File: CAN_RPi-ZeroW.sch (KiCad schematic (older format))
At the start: 32 parts, among them J1 RJ45, J2 RJ45, J3 Raspberry_Pi_2_3, SW1 SW_SPST, U1 TJA1042T/3, U2 MCP2515-I/ST, U3 MCP16301, Y1 8MHz

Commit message: PCB errors corrected and short installation guide added to README.md
Corrected errors:
- Pin header instead of socket strip used --> wrong pin layout of Raspi connector
- STB pin of transceiver not connected --> sending of messages was not possible

Now, small 26 pin connector is used instead of full 40 pin RPi HAT connector.
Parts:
- removed J3: Raspberry_Pi_2_3, Pin_Headers:Pin_Header_Straight_2x20_Pitch2.54mm, symbol Connector:Raspberry_Pi_2_3
- added J3: Raspberry_Pi_HAT_26p, Socket_Strips:Socket_Strip_Straight_2x13_Pitch2.54mm, symbol LibreSolar:Raspberry_Pi_HAT_26p
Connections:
- net +3V3: now also J3.1 (3V3), J3.17 (3V3)
- net +5V: now also J3.2 (5V), J3.4 (5V)
- net CAN_INT: now also J3.22 (GPIO25_(GEN6))
- net GND: now also J3.14 (GND), J3.20 (GND), J3.25 (GND), J3.6 (GND), J3.9 (GND)
- net LED1: now also J3.15 (GPIO22_(GEN3))
- net SPI_CE0: now also J3.24 ((~SPI_CE0~)_GPIO8)
- net SPI_MISO: now also J3.21 ((SPI_MISO)_GPIO9)
- net SPI_MOSI: now also J3.19 ((SPI_MOSI)_GPIO10)
- net SPI_SCLK: now also J3.23 ((SPI_SCLK)_GPIO11)
- net CAN_STB: now reaches U1.8 (STB)
- net CAN_STB: now also J3.18 (GPIO24_(GEN5))
- no-connect marks 1 -> 13
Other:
- moved on the sheet: U1
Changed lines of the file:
@@
-$EndComp
-$Comp
-L Connector:Raspberry_Pi_2_3 J3
-U 1 1 5A141DFA
-P 3650 8100
-F 0 "J3" H 2900 9350 50  0000 C CNN
-F 1 "Raspberry_Pi_2_3" H 4300 9350 50  0000 C CNN
-F 2 "Pin_Headers:Pin_Header_Straight_2x20_Pitch2.54mm" H 4650 9350 50  0001 C CNN
-F 3 "https://www.raspberrypi.org/documentation/hardware/raspberrypi/schematics/RPI-3B-V1_2-SCHEMATIC-REDUCED.pdf" H 3700 7950 50  0001 C CNN
-	1    3650 8100
-	1    0    0    -1
 $EndComp
 $Comp
@@
 L interface:TJA1049T-3 U1
 U 1 1 5A144F99
-P 8850 2700
-F 0 "U1" H 8500 3050 50  0000 C CNN
-F 1 "TJA1042T/3" H 9150 3050 50  0000 C CNN
-F 2 "Housings_SOIC:SOIC-8_3.9x4.9mm_Pitch1.27mm" H 8850 2200 50  0001 C CIN
-F 3 "http://www.nxp.com/documents/data_sheet/TJA1049.pdf" H 8850 2700 50  0001 C CNN
-	1    8850 2700
+P 8900 2700
+F 0 "U1" H 8550 3050 50  0000 C CNN
+F 1 "TJA1042T/3" H 9200 3050 50  0000 C CNN
+F 2 "Housings_SOIC:SOIC-8_3.9x4.9mm_Pitch1.27mm" H 8900 2200 50  0001 C CIN
+F 3 "http://www.nxp.com/documents/data_sheet/TJA1049.pdf" H 8900 2700 50  0001 C CNN
+	1    8900 2700
 	1    0    0    -1
 $EndComp
@@
 CAN_L
 Wire Wire Line
-	4550 8100 5150 8100
-Wire Wire Line
-	4550 8200 5150 8200
-Wire Wire Line
-	4550 8300 5150 8300
-Wire Wire Line
-	4550 8000 5150 8000
+	4600 8100 5200 8100
+Wire Wire Line
+	4600 8200 5200 8200
+Wire Wire Line
+	4600 8300 5200 8300
+Wire Wire Line
+	4600 8000 5200 8000
 $Comp
 L power:GND #PWR030
 U 1 1 5A15D40D
-P 3950 9650
-F 0 "#PWR030" H 3950 9400 50  0001 C CNN
-F 1 "GND" H 3955 9477 50  0000 C CNN
-F 2 "" H 3950 9650 50  0001 C CNN
-F 3 "" H 3950 9650 50  0001 C CNN
-	1    3950 9650
+P 3900 9600
+F 0 "#PWR030" H 3900 9350 50  0001 C CNN
+F 1 "GND" H 3905 9427 50  0000 C CNN
+F 2 "" H 3900 9600 50  0001 C CNN
+F 3 "" H 3900 9600 50  0001 C CNN
+	1    3900 9600
 	1    0    0    -1
 $EndComp
@@
 L power:+3.3V #PWR026
 U 1 1 5A15E50C
-P 3750 6500
-F 0 "#PWR026" H 3750 6350 50  0001 C CNN
-F 1 "+3.3V" H 3750 6640 50  0000 C CNN
-F 2 "" H 3750 6500 50  0000 C CNN
-F 3 "" H 3750 6500 50  0000 C CNN
-	1    3750 6500
+P 3800 6500
+F 0 "#PWR026" H 3800 6350 50  0001 C CNN
+F 1 "+3.3V" H 3800 6640 50  0000 C CNN
+F 2 "" H 3800 6500 50  0000 C CNN
+F 3 "" H 3800 6500 50  0000 C CNN
+	1    3800 6500
 	1    0    0    -1
 $EndComp
@@
 L power:+5V #PWR025
 U 1 1 5A15E512
-P 3450 6500
-F 0 "#PWR025" H 3450 6350 50  0001 C CNN
-F 1 "+5V" H 3450 6640 50  0000 C CNN
-F 2 "" H 3450 6500 50  0000 C CNN
-F 3 "" H 3450 6500 50  0000 C CNN
-	1    3450 6500
-	1    0    0    -1
-$EndComp
-Wire Wire Line
-	3750 6500 3750 6800
-Wire Wire Line
-	3450 6500 3450 6800
-Wire Wire Line
-	3450 6600 3550 6600
-Wire Wire Line
-	3550 6600 3550 6800
-Wire Wire Line
-	3750 6600 3850 6600
-Wire Wire Line
-	3850 6600 3850 6800
-Connection ~ 3750 6600
-Connection ~ 3450 6600
-Wire Wire Line
-	3250 9400 3250 9500
-Wire Wire Line
-	3250 9500 3950 9500
-Wire Wire Line
-	3950 9400 3950 9650
-Connection ~ 3950 9500
-Wire Wire Line
-	3850 9400 3850 9500
-Connection ~ 3850 9500
-Wire Wire Line
-	3750 9400 3750 9500
-Connection ~ 3750 9500
-Wire Wire Line
-	3650 9400 3650 9500
-Connection ~ 3650 9500
-Wire Wire Line
-	3550 9400 3550 9500
-Connection ~ 3550 9500
-Wire Wire Line
-	3450 9400 3450 9500
-Connection ~ 3450 9500
-Wire Wire Line
-	3350 9400 3350 9500
-Connection ~ 3350 9500
+P 3500 6500
+F 0 "#PWR025" H 3500 6350 50  0001 C CNN
+F 1 "+5V" H 3500 6640 50  0000 C CNN
+F 2 "" H 3500 6500 50  0000 C CNN
+F 3 "" H 3500 6500 50  0000 C CNN
+	1    3500 6500
+	1    0    0    -1
+$EndComp
+Wire Wire Line
+	3800 6500 3800 6800
+Wire Wire Line
+	3500 6500 3500 6800
+Wire Wire Line
+	3500 6600 3600 6600
+Wire Wire Line
+	3600 6600 3600 6800
+Wire Wire Line
+	3800 6600 3900 6600
+Wire Wire Line
+	3900 6600 3900 6800
+Connection ~ 3800 6600
+Connection ~ 3500 6600
+Wire Wire Line
+	3300 9400 3300 9500
+Wire Wire Line
+	3700 9400 3700 9500
+Connection ~ 3700 9500
+Wire Wire Line
+	3600 9400 3600 9500
+Connection ~ 3600 9500
+Wire Wire Line
+	3500 9400 3500 9500
+Connection ~ 3500 9500
+Wire Wire Line
+	3400 9400 3400 9500
+Connection ~ 3400 9500
 $Comp
 L power:GND #PWR022
@@
 L power:GND #PWR019
 U 1 1 5A1ACAC5
-P 8850 3200
-F 0 "#PWR019" H 8850 2950 50  0001 C CNN
-F 1 "GND" H 8855 3027 50  0000 C CNN
-F 2 "" H 8850 3200 50  0001 C CNN
-F 3 "" H 8850 3200 50  0001 C CNN
-	1    8850 3200
-	1    0    0    -1
-$EndComp
-Wire Wire Line
-	8850 3100 8850 3200
+P 8900 3200
+F 0 "#PWR019" H 8900 2950 50  0001 C CNN
+F 1 "GND" H 8905 3027 50  0000 C CNN
+F 2 "" H 8900 3200 50  0001 C CNN
+F 3 "" H 8900 3200 50  0001 C CNN
+	1    8900 3200
+	1    0    0    -1
+$EndComp
+Wire Wire Line
+	8900 3100 8900 3200
 $Comp
 L power:+5V #PWR017
 U 1 1 5A1B24A4
-P 8850 2200
-F 0 "#PWR017" H 8850 2050 50  0001 C CNN
-F 1 "+5V" H 8850 2340 50  0000 C CNN
-F 2 "" H 8850 2200 50  0000 C CNN
-F 3 "" H 8850 2200 50  0000 C CNN
-	1    8850 2200
-	1    0    0    -1
-$EndComp
-Wire Wire Line
-	8850 2300 8850 2200
+P 8900 2200
+F 0 "#PWR017" H 8900 2050 50  0001 C CNN
+F 1 "+5V" H 8900 2340 50  0000 C CNN
+F 2 "" H 8900 2200 50  0000 C CNN
+F 3 "" H 8900 2200 50  0000 C CNN
+	1    8900 2200
+	1    0    0    -1
+$EndComp
+Wire Wire Line
+	8900 2300 8900 2200
 Wire Wire Line
 	4300 2400 4750 2400
@@
 TXCAN
 Wire Wire Line
-	8350 2500 8050 2500
-Wire Wire Line
-	8350 2600 8050 2600
-Text Label 8050 2500 0    50   ~ 0
+	8400 2500 8100 2500
+Wire Wire Line
+	8400 2600 8100 2600
+Text Label 8100 2500 0    50   ~ 0
 TXCAN
-Text Label 8050 2600 0    50   ~ 0
+Text Label 8100 2600 0    50   ~ 0
 RXCAN
-Text Label 5150 8000 2    50   ~ 0
+Text Label 5200 8000 2    50   ~ 0
 SPI_CE0
-Text Label 5150 8100 2    50   ~ 0
+Text Label 5200 8100 2    50   ~ 0
 SPI_MISO
-Text Label 5150 8200 2    50   ~ 0
+Text Label 5200 8200 2    50   ~ 0
 SPI_MOSI
-Text Label 5150 8300 2    50   ~ 0
+Text Label 5200 8300 2    50   ~ 0
 SPI_SCLK
 Wire Wire Line
-	2750 8000 2150 8000
-Text Label 2150 8000 0    50   ~ 0
+	2800 8000 2200 8000
+Text Label 2200 8000 0    50   ~ 0
 LED1
 $Comp
@@
 SPI_MOSI
 Wire Wire Line
-	2750 8300 2150 8300
-Text Label 2150 8300 0    50   ~ 0
+	2800 8300 2200 8300
+Text Label 2200 8300 0    50   ~ 0
 CAN_INT
 Wire Wire Line
@@
 	1800 2650 1800 2550
 Wire Wire Line
-	9350 2600 9900 2600
-Wire Wire Line
-	9350 2800 9900 2800
-Text Label 9900 2800 2    50   ~ 0
+	9400 2600 9950 2600
+Wire Wire Line
+	9400 2800 9950 2800
+Text Label 9950 2800 2    50   ~ 0
 CAN_L
-Text Label 9900 2600 2    50   ~ 0
+Text Label 9950 2600 2    50   ~ 0
 CAN_H
 $Comp
@@
 TX0BF
 Wire Wire Line
-	8350 2800 7850 2800
-Wire Wire Line
-	7850 2700 7850 2800
+	8400 2800 7900 2800
+Wire Wire Line
+	7900 2700 7900 2800
 $Comp
 L power:+3.3V #PWR018
 U 1 1 5A2E151E
-P 7850 2700
-F 0 "#PWR018" H 7850 2550 50  0001 C CNN
-F 1 "+3.3V" H 7850 2840 50  0000 C CNN
-F 2 "" H 7850 2700 50  0000 C CNN
-F 3 "" H 7850 2700 50  0000 C CNN
-	1    7850 2700
+P 7900 2700
+F 0 "#PWR018" H 7900 2550 50  0001 C CNN
+F 1 "+3.3V" H 7900 2840 50  0000 C CNN
+F 2 "" H 7900 2700 50  0000 C CNN
+F 3 "" H 7900 2700 50  0000 C CNN
+	1    7900 2700
 	1    0    0    -1
 $EndComp
@@
 Text Notes 11000 1400 0    100  ~ 0
 ESD protection + Connector
+Wire Wire Line
+	8400 2900 8000 2900
+Text Label 8000 2900 0    50   ~ 0
+CAN_STB
+Wire Wire Line
+	2800 8200 2200 8200
+Text Label 2200 8200 0    50   ~ 0
+CAN_STB
+$Comp
+L LibreSolar:Raspberry_Pi_HAT_26p J3
+U 1 1 5A3B347A
+P 3700 8100
+F 0 "J3" H 2950 9350 50  0000 C CNN
+F 1 "Raspberry_Pi_HAT_26p" H 4500 9350 50  0000 C CNN
+F 2 "Socket_Strips:Socket_Strip_Straight_2x13_Pitch2.54mm" H 4700 9350 50  0001 C CNN
+F 3 "https://www.raspberrypi.org/documentation/hardware/raspberrypi/schematics/RPI-3B-V1_2-SCHEMATIC-REDUCED.pdf" H 3750 7950 50  0001 C CNN
+	1    3700 8100
+	1    0    0    -1
+$EndComp
+NoConn ~ 4600 7400
+NoConn ~ 4600 7300
+NoConn ~ 4600 7200
+NoConn ~ 4600 7900
+NoConn ~ 2800 8100
+NoConn ~ 2800 7700
+NoConn ~ 2800 7600
+NoConn ~ 2800 7500
+NoConn ~ 4600 8800
+NoConn ~ 4600 8900
+Wire Wire Line
+	3300 9500 3900 9500
+Wire Wire Line
+	3900 9500 3900 9600
+NoConn ~ 13000 4700
+NoConn ~ 13000 3100
 $EndSCHEMATC

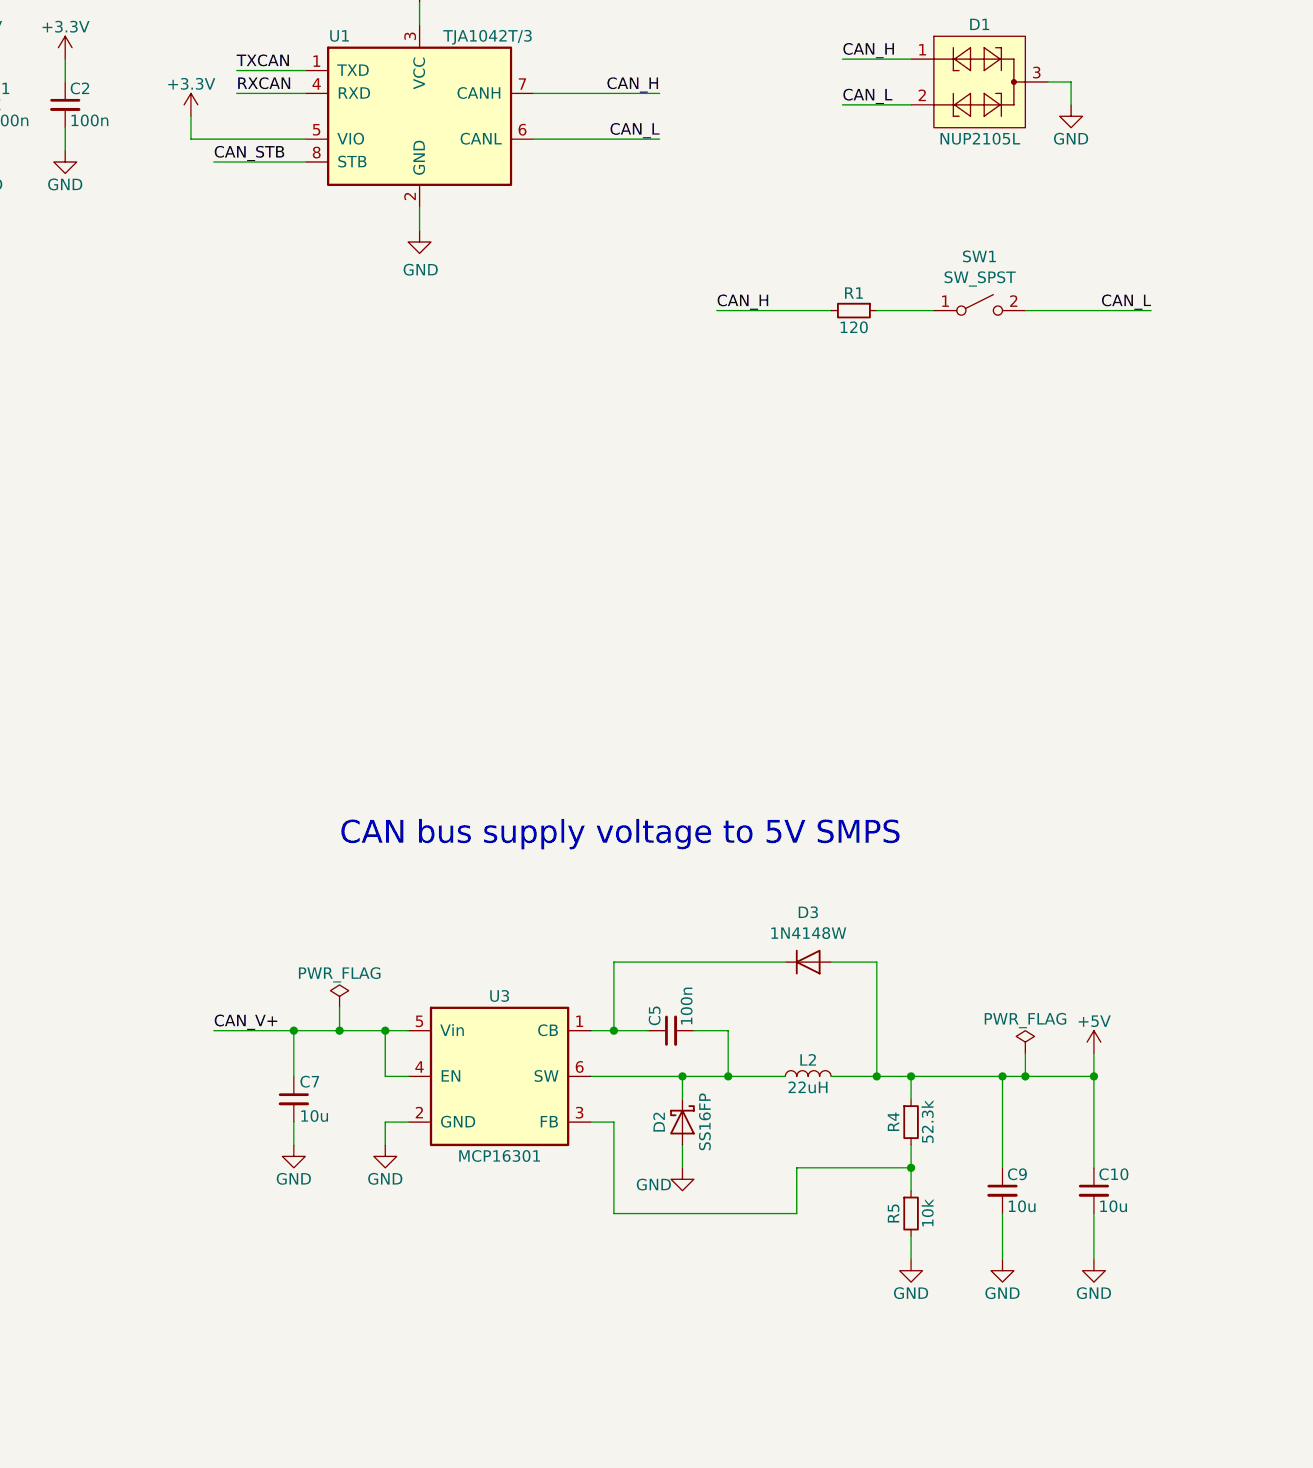
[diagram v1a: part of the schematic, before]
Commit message: Pull-down resistor for transceiver STB pin added.
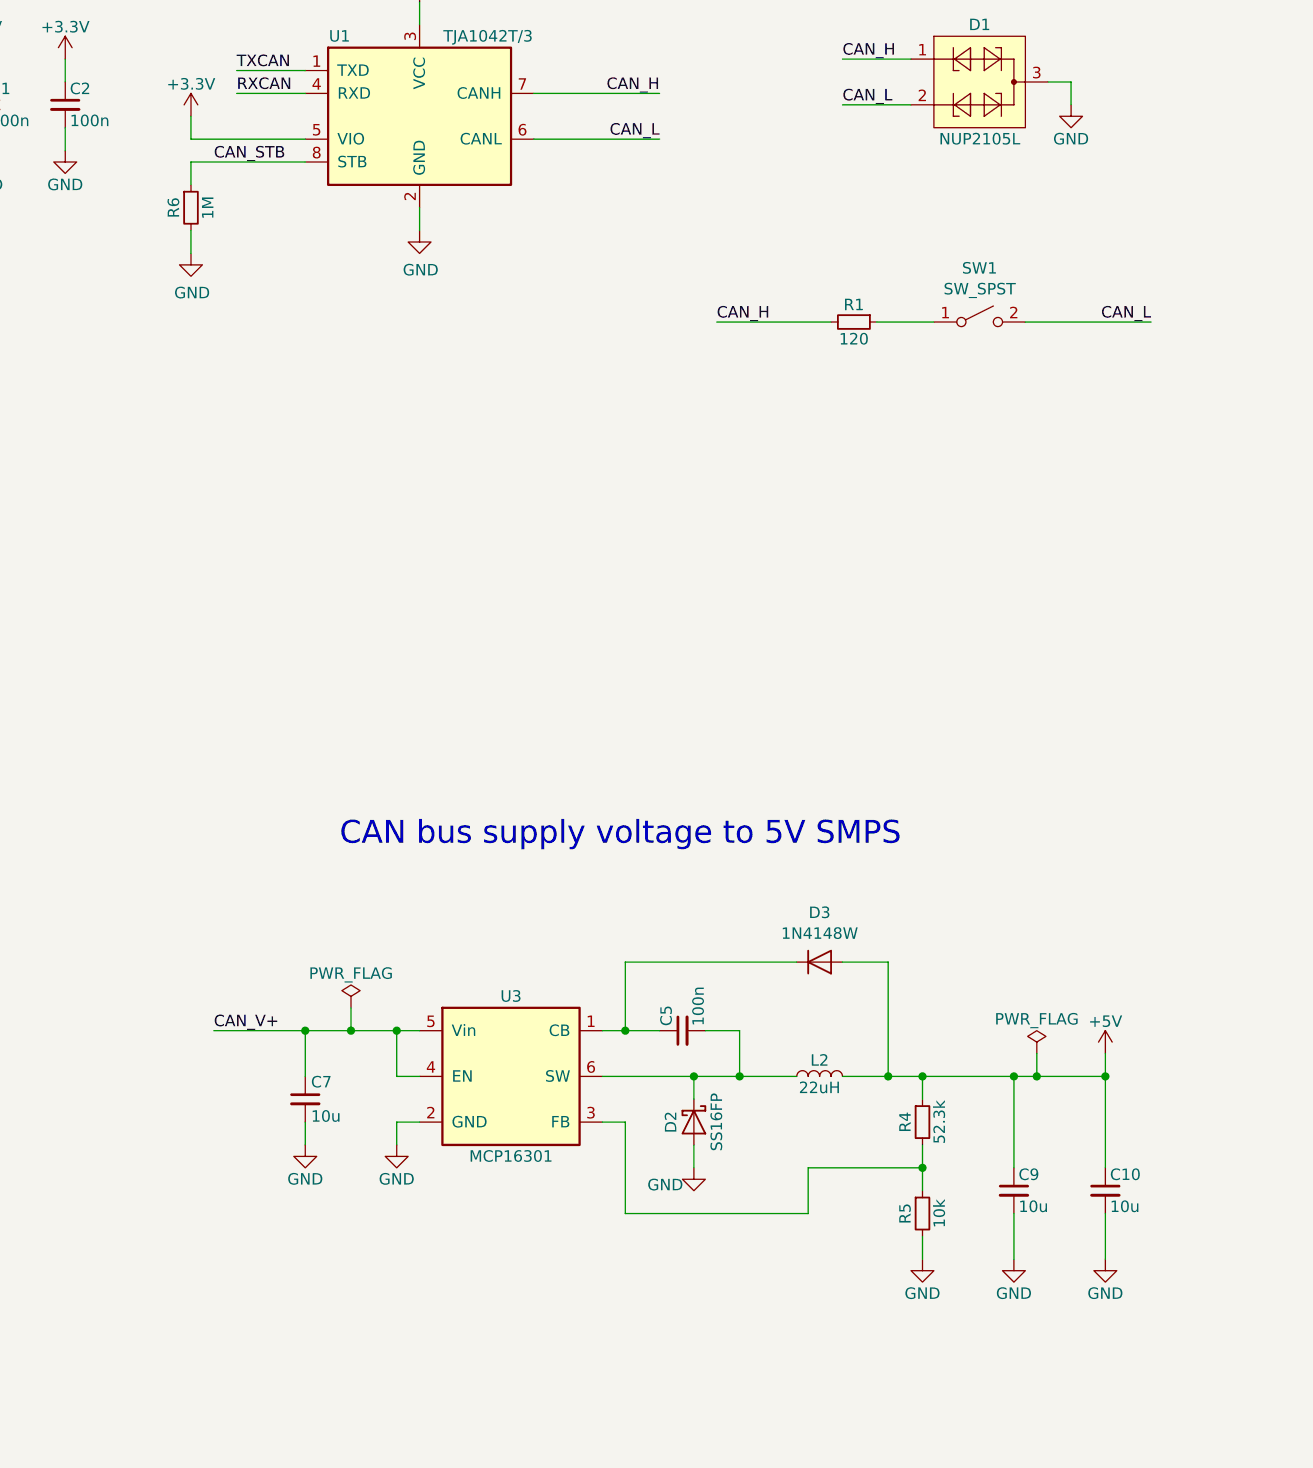
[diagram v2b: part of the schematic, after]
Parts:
- added R6: 1M, LibreSolar:R_0603_1608, symbol IEC-60617:R
- R1: PartNumber RC1206FR-07120L -> RC1206FR-07120RL
- R5: PartNumber RC0603FR-07150KL -> RC0603FR-0710KL
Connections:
- net CAN_STB: now also R6.1
- net GND: now also R6.2
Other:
- moved on the sheet: C10, C5, C7, C9, D2, D3, L2, R1, R4, R5, SW1, U3
